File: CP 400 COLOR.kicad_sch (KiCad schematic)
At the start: 171 parts, among them CN1 CN9, CN10 CN10, CN13 CN13, CN14 CN14, CN2 CASSETE, CN3 CN8, CN4 RS232, CN5 JOYESQ, CN6 JOYDIR, CN8 CN12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

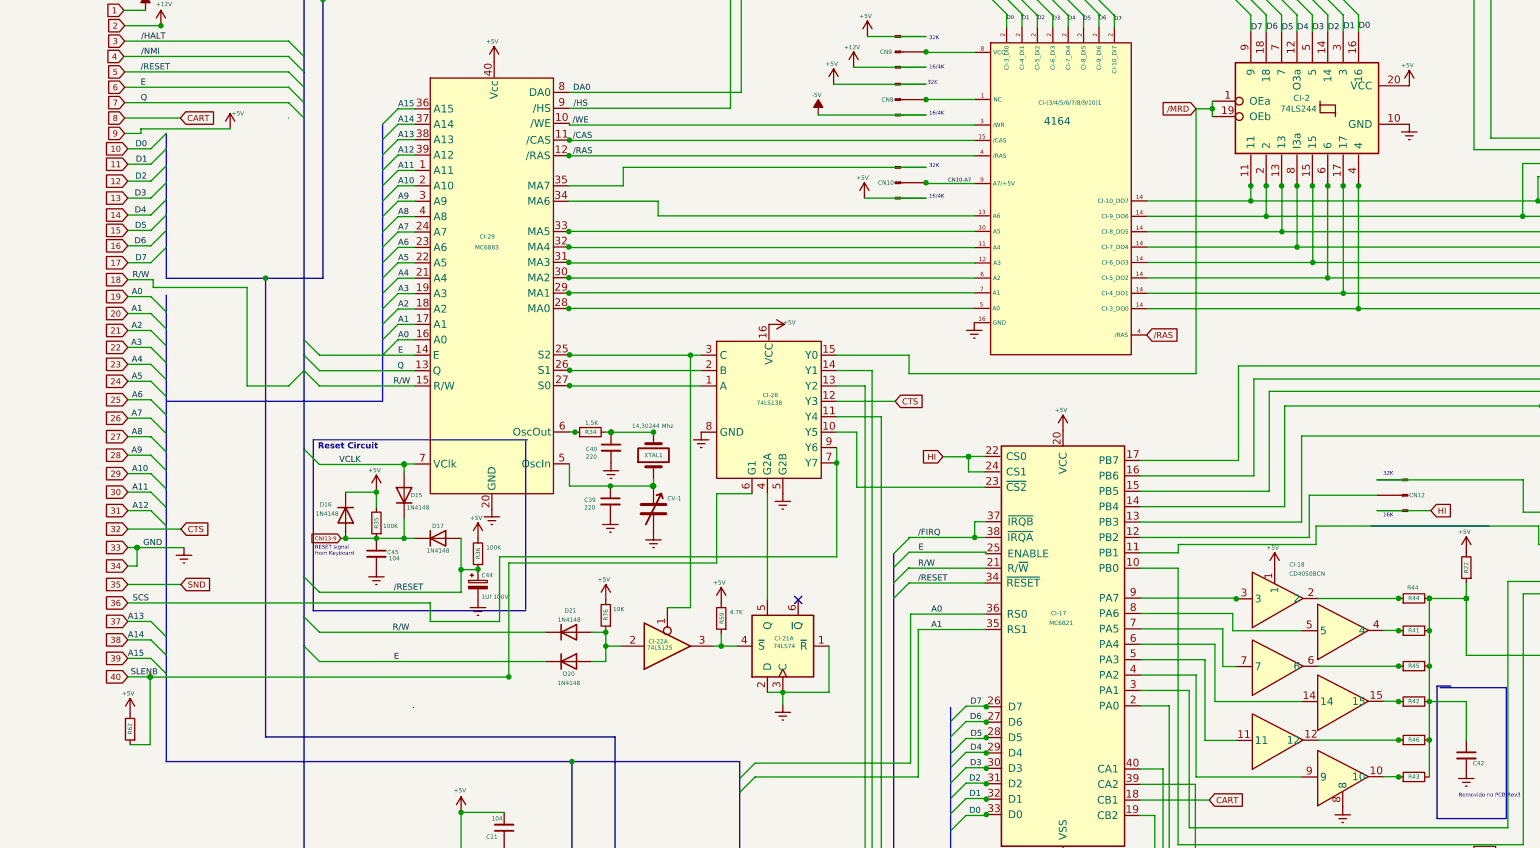
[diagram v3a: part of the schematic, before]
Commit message: Add more values to components
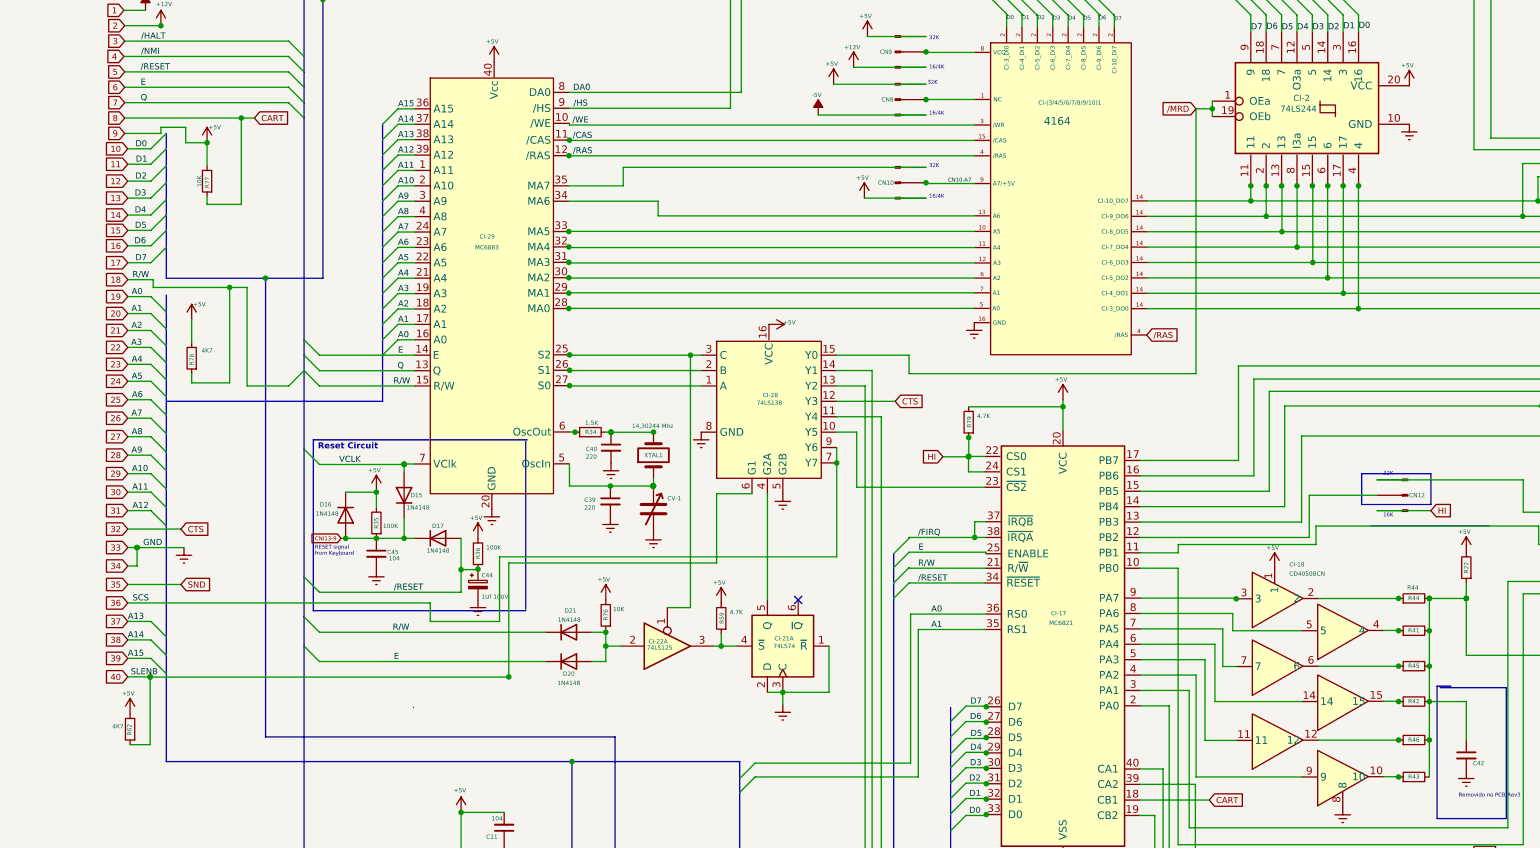
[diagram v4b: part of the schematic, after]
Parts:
- added R77: 10K, Resistor_THT:R_Axial_DIN0207_L6.3mm_D2.5mm_P7.62mm_Horizontal, symbol Device:R_Small
- added R78: 4K7, Resistor_THT:R_Axial_DIN0207_L6.3mm_D2.5mm_P2.54mm_Vertical, symbol Device:R_Small
- added R79: 4.7K, Resistor_THT:R_Axial_DIN0207_L6.3mm_D2.5mm_P2.54mm_Vertical, symbol Device:R_Small
- R62: value R62 -> 4K7
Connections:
- net +5V: now also R77.2, R78.2, R79.2
- net 18: now also R78.1
- net 8: now also R77.1
- net HI: now also R79.1
